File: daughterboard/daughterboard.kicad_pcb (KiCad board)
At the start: 2 copper layers, 45.7 x 56 mm, 40 parts, among them CON1 12V_JACK, IC1 ATMEGA328P-A, P1 X_PB01, P2 X_PC1, P3 CONN_13X2, P4 AZIMUTH, P5 ELEVATION, P6 X_ADC67, P7 VALVE, P8 X_PD4567, Q1 TIP120, U1 ULN2803A, Y1 8MHz

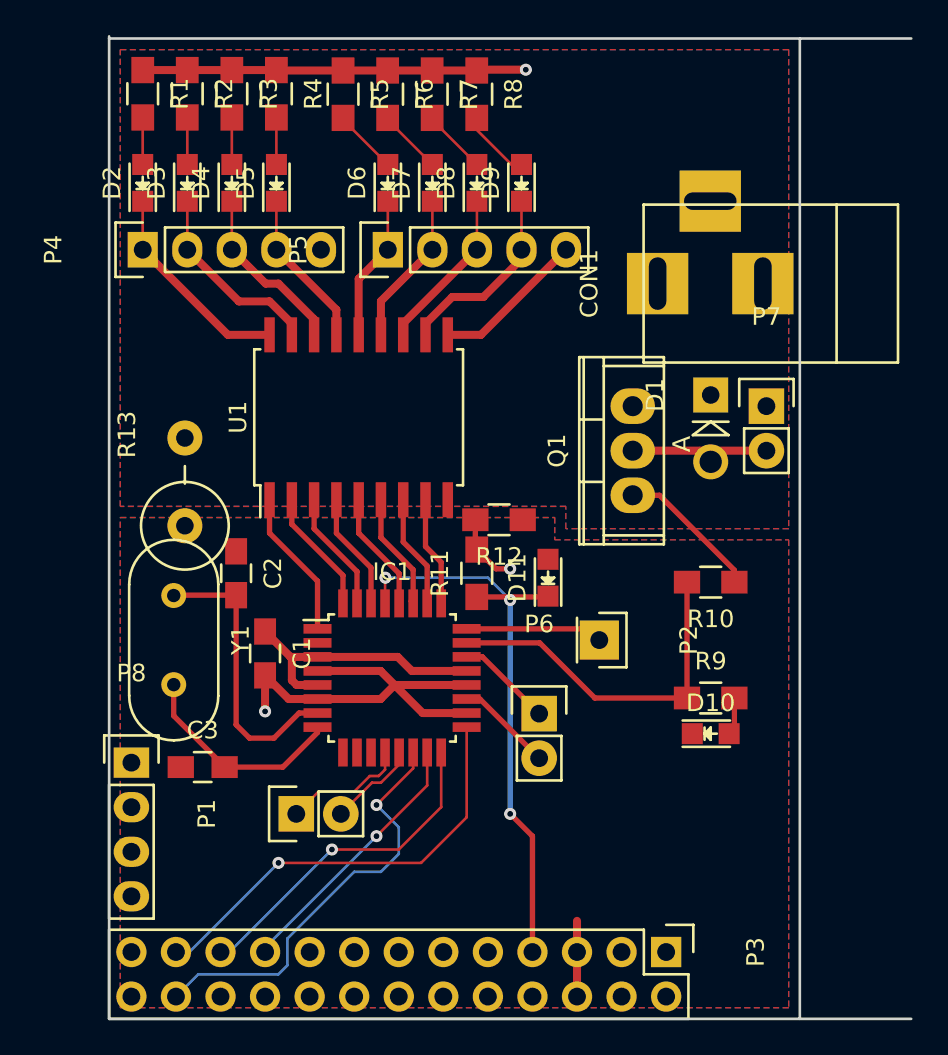
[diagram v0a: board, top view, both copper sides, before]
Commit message: Slightly increase board size, extend ground/power planes up to edge cuts
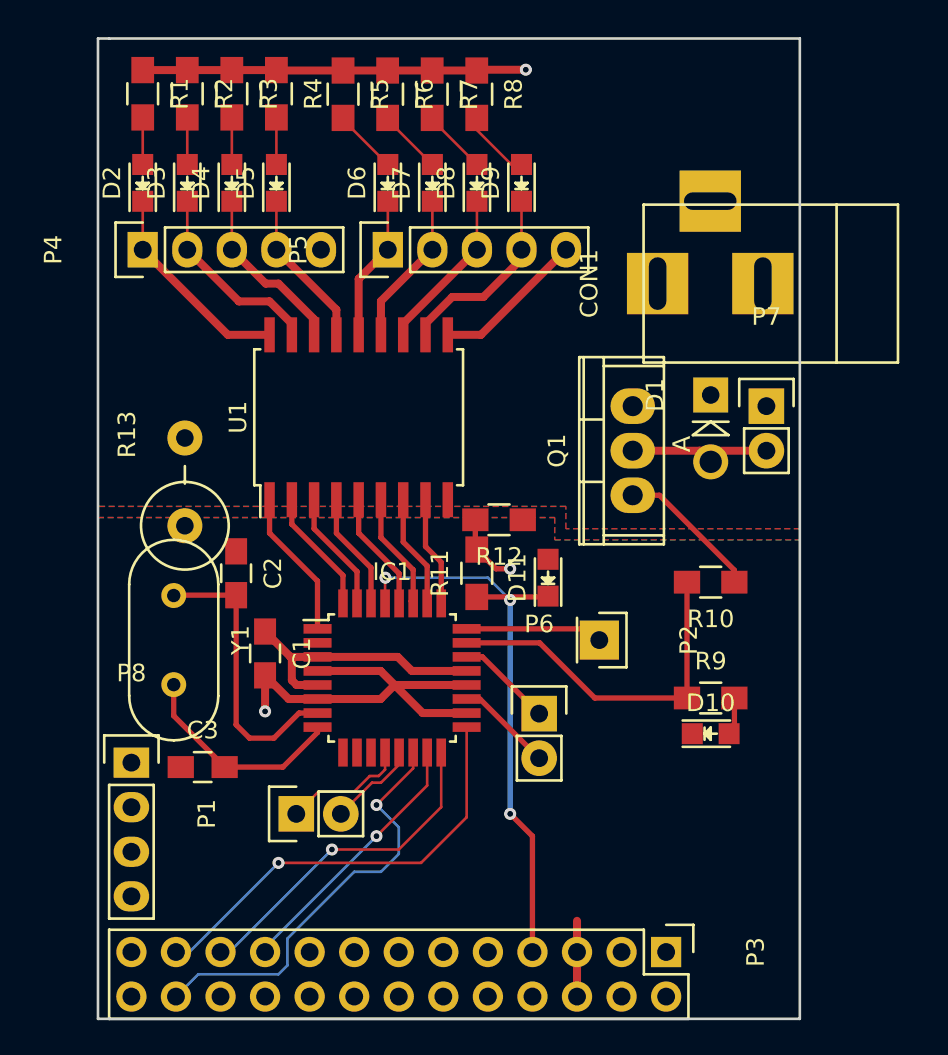
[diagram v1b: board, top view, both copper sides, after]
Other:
- board size 45.7 x 56 mm -> 40 x 55.9 mm
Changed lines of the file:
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@@
     (links 92)
     (no_connects 7)
-    (area 143.424999 124.924999 189.295001 181.075001)
+    (area 143.424999 125.044999 182.945001 181.075001)
     (thickness 1.6)
-    (drawings 37)
+    (drawings 39)
     (tracks 195)
     (zones 0)
@@
       (net 1 GND))
   )
-  (gr_line (start 189.22 125.12) (end 143.5 125.12) (angle 90) (layer Edge.Cuts) (width 0.15))
-  (gr_line (start 182.87 181) (end 182.87 125.12) (angle 90) (layer Edge.Cuts) (width 0.15))
-  (gr_line (start 143.5 181) (end 189.22 181) (angle 90) (layer Edge.Cuts) (width 0.15))
+  (gr_line (start 142.865 125.12) (end 143.5 125.12) (angle 90) (layer Edge.Cuts) (width 0.15))
+  (gr_line (start 142.865 181) (end 142.865 125.12) (angle 90) (layer Edge.Cuts) (width 0.15))
+  (gr_line (start 143.5 181) (end 142.865 181) (angle 90) (layer Edge.Cuts) (width 0.15))
+  (gr_line (start 143.5 125.12) (end 182.87 125.12) (angle 90) (layer Edge.Cuts) (width 0.15))
+  (gr_line (start 182.87 181) (end 143.5 181) (angle 90) (layer Edge.Cuts) (width 0.15))
+  (gr_line (start 182.87 125.12) (end 182.87 181) (angle 90) (layer Edge.Cuts) (width 0.15))
   (gr_text "RASPBERRY-PI ADDON BOARD\nVIEW FROM TOP\nNOTE: P1 SHOULD BE FITTED ON THE REVERSE OF THE BOARD" (at 144 183.5) (layer Dwgs.User)
     (effects (font (size 2 1.7) (thickness 0.12)) (justify left))
@@
   (gr_line (start 194.5 138) (end 194.5 125) (angle 90) (layer Dwgs.User) (width 0.2))
   (gr_line (start 182.5 125) (end 182.5 138) (angle 90) (layer Dwgs.User) (width 0.2))
-  (gr_line (start 143.5 125) (end 143.5 181) (angle 90) (layer Edge.Cuts) (width 0.15))
   (segment (start 155.379 160.369) (end 159.953 160.369) (width 0.4572) (layer F.Cu) (net 2))
   (segment (start 160.753 161.169) (end 163.879 161.169) (width 0.4572) (layer F.Cu) (net 2))
@@
     (polygon
       (pts
-        (xy 144.135 125.755) (xy 182.235 125.755) (xy 182.235 153.06) (xy 169.535 153.06) (xy 169.535 151.79)
-        (xy 144.135 151.79)
+        (xy 142.865 125.12) (xy 182.87 125.12) (xy 182.87 153.06) (xy 169.535 153.06) (xy 169.535 151.79)
+        (xy 142.865 151.79)
       )
     )
@@
     (polygon
       (pts
-        (xy 144.135 125.755) (xy 182.235 125.755) (xy 182.235 153.06) (xy 169.535 153.06) (xy 169.535 151.79)
-        (xy 144.135 151.79)
+        (xy 142.865 125.12) (xy 182.87 125.12) (xy 182.87 153.06) (xy 169.535 153.06) (xy 169.535 151.79)
+        (xy 142.865 151.79)
       )
     )
@@
     (polygon
       (pts
-        (xy 144.135 152.425) (xy 168.9 152.425) (xy 168.9 153.695) (xy 182.235 153.695) (xy 182.235 180.365)
-        (xy 144.135 180.365)
+        (xy 142.865 152.425) (xy 168.9 152.425) (xy 168.9 153.695) (xy 182.87 153.695) (xy 182.87 181)
+        (xy 142.865 181)
       )
     )
@@
     (polygon
       (pts
-        (xy 144.135 152.425) (xy 168.9 152.425) (xy 168.9 153.695) (xy 182.235 153.695) (xy 182.235 180.365)
-        (xy 144.135 180.365)
+        (xy 142.865 152.425) (xy 168.9 152.425) (xy 168.9 153.695) (xy 182.87 153.695) (xy 182.87 181)
+        (xy 142.865 181)
       )
     )
